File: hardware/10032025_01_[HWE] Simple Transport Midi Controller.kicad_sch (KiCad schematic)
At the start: 0 parts

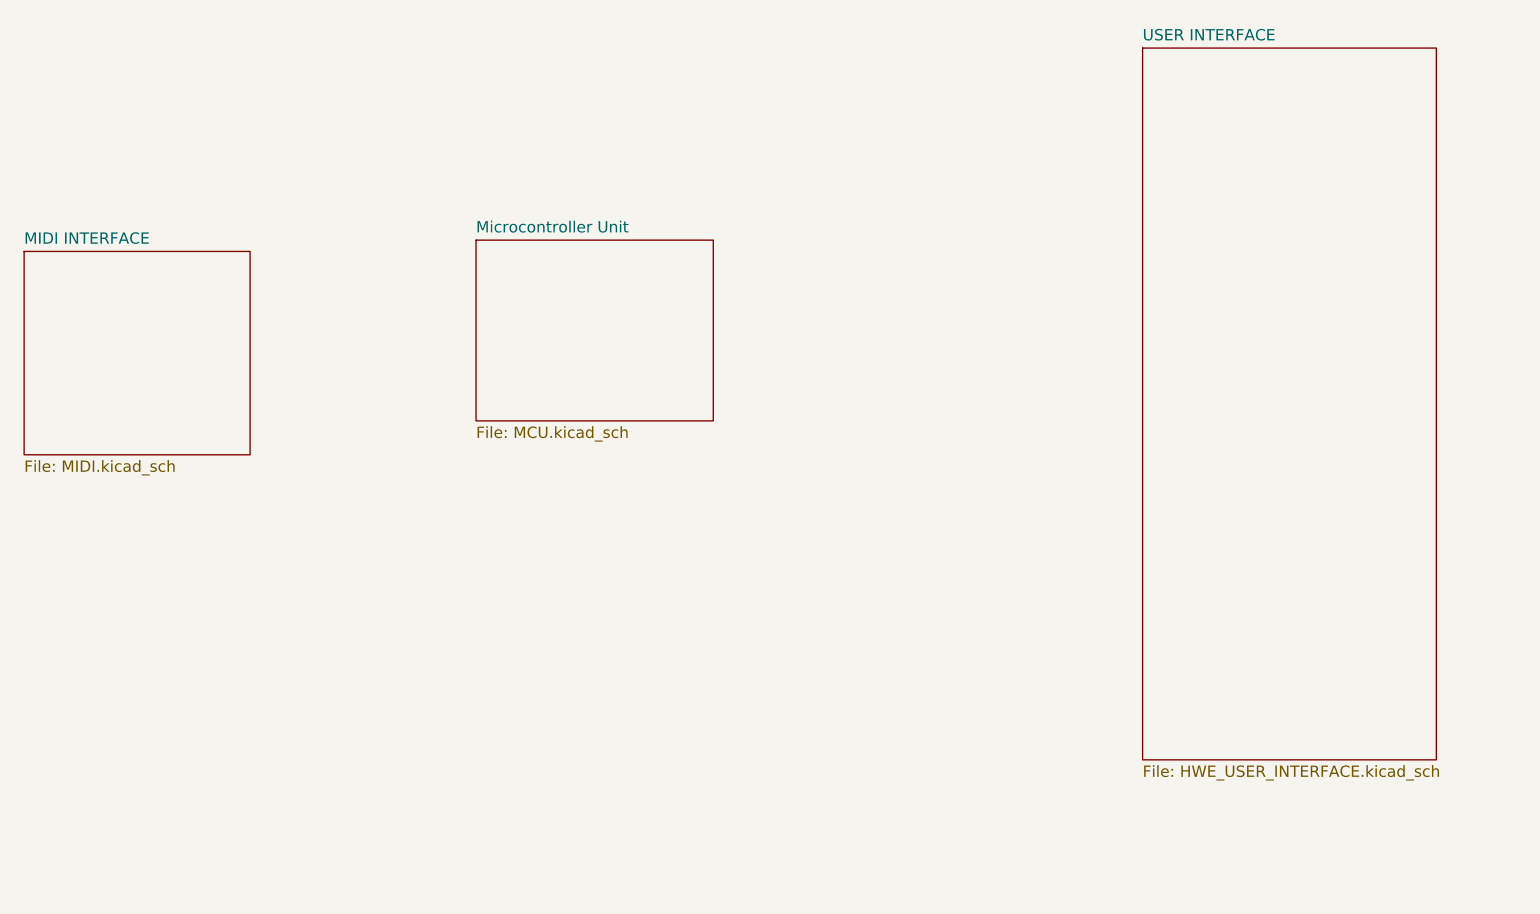
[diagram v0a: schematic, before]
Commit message: feat: Created Button I2C Interfaces
For now, all we are using is generic 1x5 Connectors following the DFR Robot's RGB Button pinout https://wiki.dfrobot.com/SKU_DFR0991_Gravity_I2C_RGB_LED_Button_Module#target_9
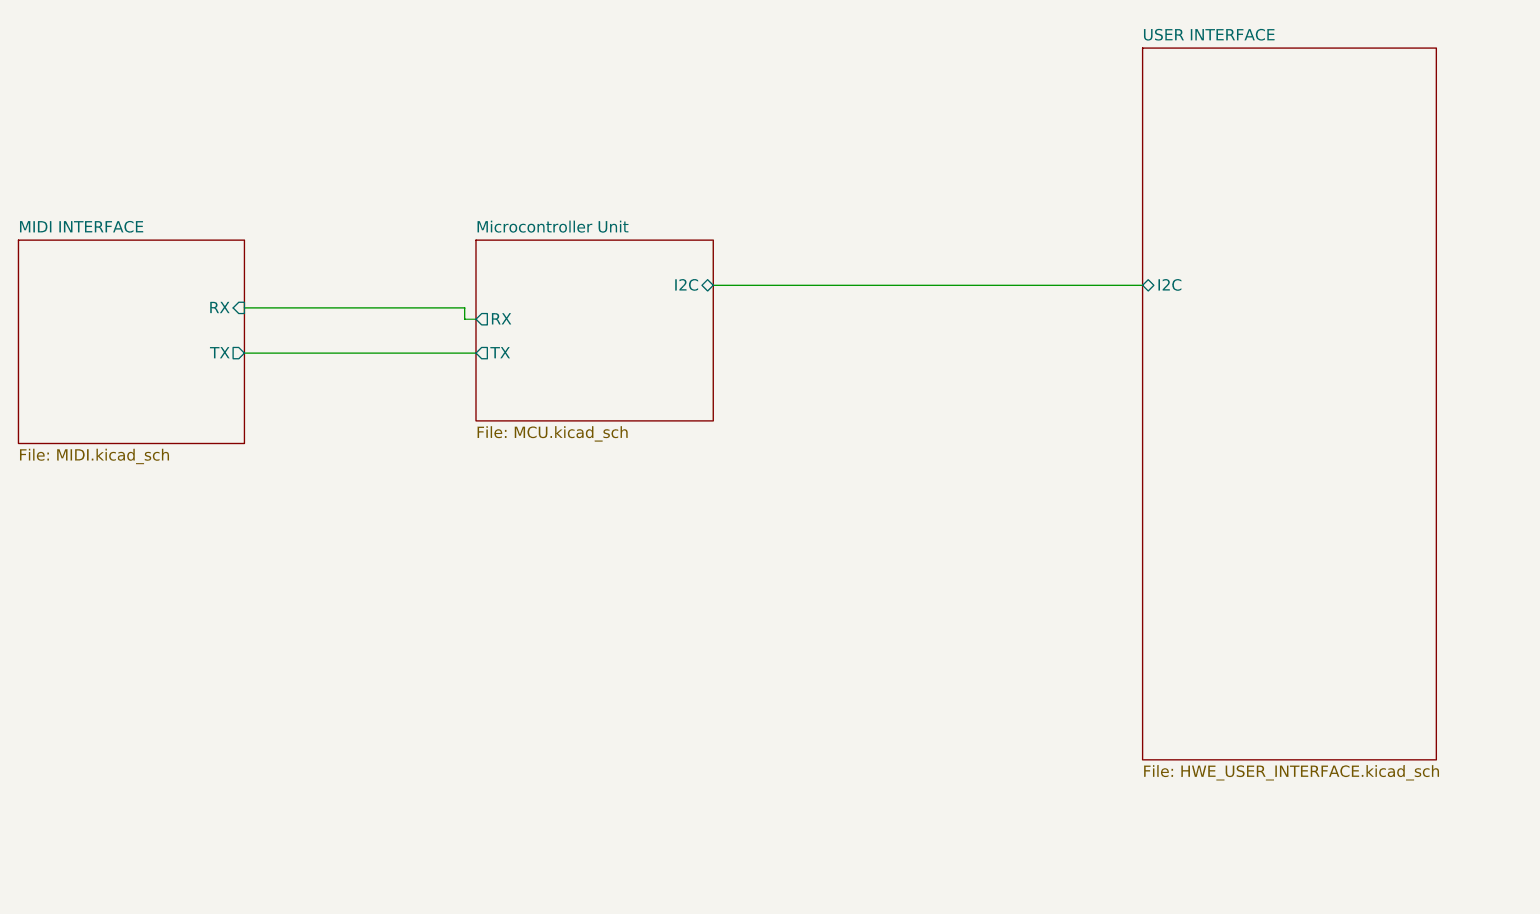
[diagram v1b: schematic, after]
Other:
- sheet MIDI INTERFACE ports: added RX, TX; removed none
- sheet Microcontroller Unit ports: added I2C, RX, TX; removed none
- sheet USER INTERFACE ports: added I2C; removed none
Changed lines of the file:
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@@
 	(generator_version "9.0")
 	(paper "A4")
+	(wire
+		(pts
+			(xy 87.63 77.47) (xy 88.9 77.47)
+		)
+		(stroke
+			(width 0)
+			(type default)
+		)
+	)
+	(wire
+		(pts
+			(xy 87.63 77.47) (xy 87.63 76.2)
+		)
+		(stroke
+			(width 0)
+			(type default)
+		)
+	)
+	(wire
+		(pts
+			(xy 115.57 73.66) (xy 163.83 73.66)
+		)
+		(stroke
+			(width 0)
+			(type default)
+		)
+	)
+	(wire
+		(pts
+			(xy 87.63 76.2) (xy 62.865 76.2)
+		)
+		(stroke
+			(width 0)
+			(type default)
+		)
+	)
+	(wire
+		(pts
+			(xy 62.865 81.28) (xy 88.9 81.28)
+		)
+		(stroke
+			(width 0)
+			(type default)
+		)
+	)
 	(sheet
-		(at 38.1 69.85)
+		(at 37.465 68.58)
 		(size 25.4 22.86)
 		(exclude_from_sim no)
@@
 		)
 		(property "Sheetname" "MIDI INTERFACE"
-			(at 38.1 69.1384 0)
+			(at 37.465 67.8684 0)
 			(effects
 				(font
@@
 		)
 		(property "Sheetfile" "MIDI.kicad_sch"
-			(at 38.1 93.2946 0)
+			(at 37.465 92.0246 0)
 			(effects
 				(font
@@
 				)
 				(justify left top)
+			)
+		)
+		(pin "RX" input
+			(at 62.865 76.2 0)
+			(effects
+				(font
+					(size 1.27 1.27)
+				)
+				(justify right)
+			)
+		)
+		(pin "TX" output
+			(at 62.865 81.28 0)
+			(effects
+				(font
+					(size 1.27 1.27)
+				)
+				(justify right)
 			)
 		)
@@
 			)
 		)
+		(pin "I2C" bidirectional
+			(at 115.57 73.66 0)
+			(effects
+				(font
+					(size 1.27 1.27)
+				)
+				(justify right)
+			)
+		)
+		(pin "RX" output
+			(at 88.9 77.47 180)
+			(effects
+				(font
+					(size 1.27 1.27)
+				)
+				(justify left)
+			)
+		)
+		(pin "TX" output
+			(at 88.9 81.28 180)
+			(effects
+				(font
+					(size 1.27 1.27)
+				)
+				(justify left)
+			)
+		)
 		(instances
 			(project "10032025_01_[HWE] Simple Transport Midi Controller"
@@
 			)
 		)
+		(pin "I2C" bidirectional
+			(at 163.83 73.66 180)
+			(effects
+				(font
+					(size 1.27 1.27)
+				)
+				(justify left)
+			)
+		)

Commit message: feat: Added Volume and Inf Scroll Encoders
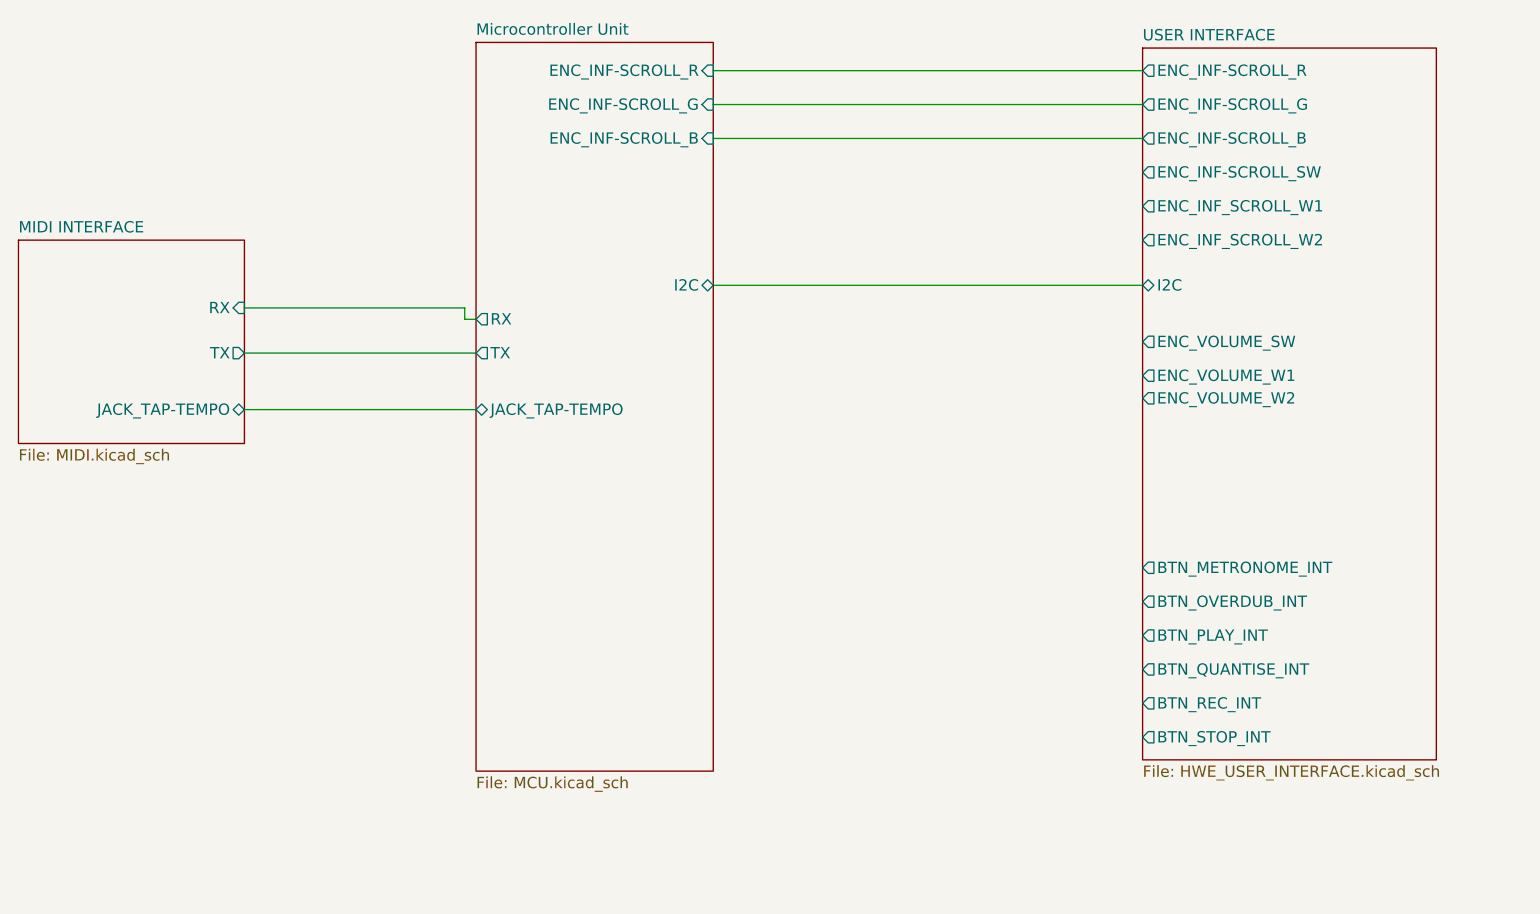
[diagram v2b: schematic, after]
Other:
- sheet MIDI INTERFACE ports: added JACK_TAP-TEMPO; removed none
- sheet Microcontroller Unit ports: added ENC_INF-SCROLL_B, ENC_INF-SCROLL_G, ENC_INF-SCROLL_R, JACK_TAP-TEMPO; removed none
- sheet USER INTERFACE ports: added BTN_METRONOME_INT, BTN_OVERDUB_INT, BTN_PLAY_INT, BTN_QUANTISE_INT, BTN_REC_INT, BTN_STOP_INT, ENC_INF-SCROLL_B, ENC_INF-SCROLL_G, ENC_INF-SCROLL_R, ENC_INF-SCROLL_SW, ENC_INF_SCROLL_W1, ENC_INF_SCROLL_W2, ENC_VOLUME_SW, ENC_VOLUME_W1, ENC_VOLUME_W2; removed none
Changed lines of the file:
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@@
+	(wire
+		(pts
+			(xy 62.865 87.63) (xy 88.9 87.63)
+		)
+		(stroke
+			(width 0)
+			(type default)
+		)
+	)
 	(wire
 		(pts
@@
 		(pts
 			(xy 87.63 76.2) (xy 62.865 76.2)
+		)
+		(stroke
+			(width 0)
+			(type default)
+		)
+	)
+	(wire
+		(pts
+			(xy 115.57 53.34) (xy 163.83 53.34)
+		)
+		(stroke
+			(width 0)
+			(type default)
+		)
+	)
+	(wire
+		(pts
+			(xy 115.57 49.53) (xy 163.83 49.53)
+		)
+		(stroke
+			(width 0)
+			(type default)
+		)
+	)
+	(wire
+		(pts
+			(xy 115.57 57.15) (xy 163.83 57.15)
 		)
 		(stroke
@@
 			)
 		)
+		(pin "JACK_TAP-TEMPO" bidirectional
+			(at 62.865 87.63 0)
+			(effects
+				(font
+					(size 1.27 1.27)
+				)
+				(justify right)
+			)
+		)
 		(instances
 			(project "10032025_01_[HWE] Simple Transport Midi Controller"
@@
 	)
 	(sheet
-		(at 88.9 68.58)
-		(size 26.67 20.32)
+		(at 88.9 46.355)
+		(size 26.67 81.915)
 		(exclude_from_sim no)
 		(in_bom yes)
@@
 		)
 		(property "Sheetname" "Microcontroller Unit"
-			(at 88.9 67.8684 0)
+			(at 88.9 45.6434 0)
 			(effects
 				(font
@@
 		)
 		(property "Sheetfile" "MCU.kicad_sch"
-			(at 88.9 89.4846 0)
+			(at 88.9 128.8546 0)
 			(effects
 				(font
@@
 		(pin "TX" output
 			(at 88.9 81.28 180)
+			(effects
+				(font
+					(size 1.27 1.27)
+				)
+				(justify left)
+			)
+		)
+		(pin "ENC_INF-SCROLL_B" input
+			(at 115.57 57.15 0)
+			(effects
+				(font
+					(size 1.27 1.27)
+				)
+				(justify right)
+			)
+		)
+		(pin "ENC_INF-SCROLL_G" input
+			(at 115.57 53.34 0)
+			(effects
+				(font
+					(size 1.27 1.27)
+				)
+				(justify right)
+			)
+		)
+		(pin "ENC_INF-SCROLL_R" input
+			(at 115.57 49.53 0)
+			(effects
+				(font
+					(size 1.27 1.27)
+				)
+				(justify right)
+			)
+		)
+		(pin "JACK_TAP-TEMPO" bidirectional
+			(at 88.9 87.63 180)
 			(effects
 				(font
@@
 			(effects
 				(font
+					(size 1.27 1.27)
+				)
+				(justify left)
+			)
+		)
+		(pin "BTN_METRONOME_INT" output
+			(at 163.83 105.41 180)
+			(effects
+				(font
+					(size 1.27 1.27)
+				)
+				(justify left)
+			)
+		)
+		(pin "BTN_OVERDUB_INT" output
+			(at 163.83 109.22 180)
+			(effects
+				(font
+					(size 1.27 1.27)
+				)
+				(justify left)
+			)
+		)
+		(pin "BTN_PLAY_INT" output
+			(at 163.83 113.03 180)
+			(effects
+				(font
+					(size 1.27 1.27)
+				)
+				(justify left)
+			)
+		)
+		(pin "BTN_QUANTISE_INT" output
+			(at 163.83 116.84 180)
+			(effects
+				(font
+					(size 1.27 1.27)
+				)
+				(justify left)
+			)
+		)
+		(pin "BTN_REC_INT" output
+			(at 163.83 120.65 180)
+			(effects
+				(font
+					(size 1.27 1.27)
+				)
+				(justify left)
+			)
+		)
+		(pin "BTN_STOP_INT" output
+			(at 163.83 124.46 180)
+			(effects
+				(font
+					(size 1.27 1.27)
+				)
+				(justify left)
+			)
+		)
+		(pin "ENC_INF-SCROLL_B" output
+			(at 163.83 57.15 180)
+			(effects
+				(font
+					(size 1.27 1.27)
+				)
+				(justify left)
+			)
+		)
+		(pin "ENC_INF-SCROLL_G" output
+			(at 163.83 53.34 180)
+			(effects
+				(font
+					(size 1.27 1.27)
+				)
+				(justify left)
+			)
+		)
+		(pin "ENC_INF-SCROLL_R" output
+			(at 163.83 49.53 180)
+			(effects
+				(font
+					(size 1.27 1.27)
+				)
+				(justify left)
+			)
+		)
+		(pin "ENC_INF-SCROLL_SW" output
+			(at 163.83 60.96 180)
+			(effects
+				(font
+					(size 1.27 1.27)
+				)
+				(justify left)
+			)
+		)
+		(pin "ENC_INF_SCROLL_W1" output
+			(at 163.83 64.77 180)
+			(effects
+				(font
+					(size 1.27 1.27)
+				)
+				(justify left)
+			)
+		)
+		(pin "ENC_INF_SCROLL_W2" output
+			(at 163.83 68.58 180)
+			(effects
+				(font
+					(size 1.27 1.27)
+				)
+				(justify left)
+			)
+		)
+		(pin "ENC_VOLUME_SW" output
+			(at 163.83 80.01 180)
+			(effects
+				(font
+					(size 1.27 1.27)
+				)
+				(justify left)
+			)
+		)
+		(pin "ENC_VOLUME_W1" output
+			(at 163.83 83.82 180)
+			(effects
+				(font
+					(size 1.27 1.27)
+				)
+				(justify left)
+			)
+		)
+		(pin "ENC_VOLUME_W2" output
+			(at 163.83 86.36 180)
+			(effects
+				(font

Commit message: feat: Connected main HW UI components to MCU
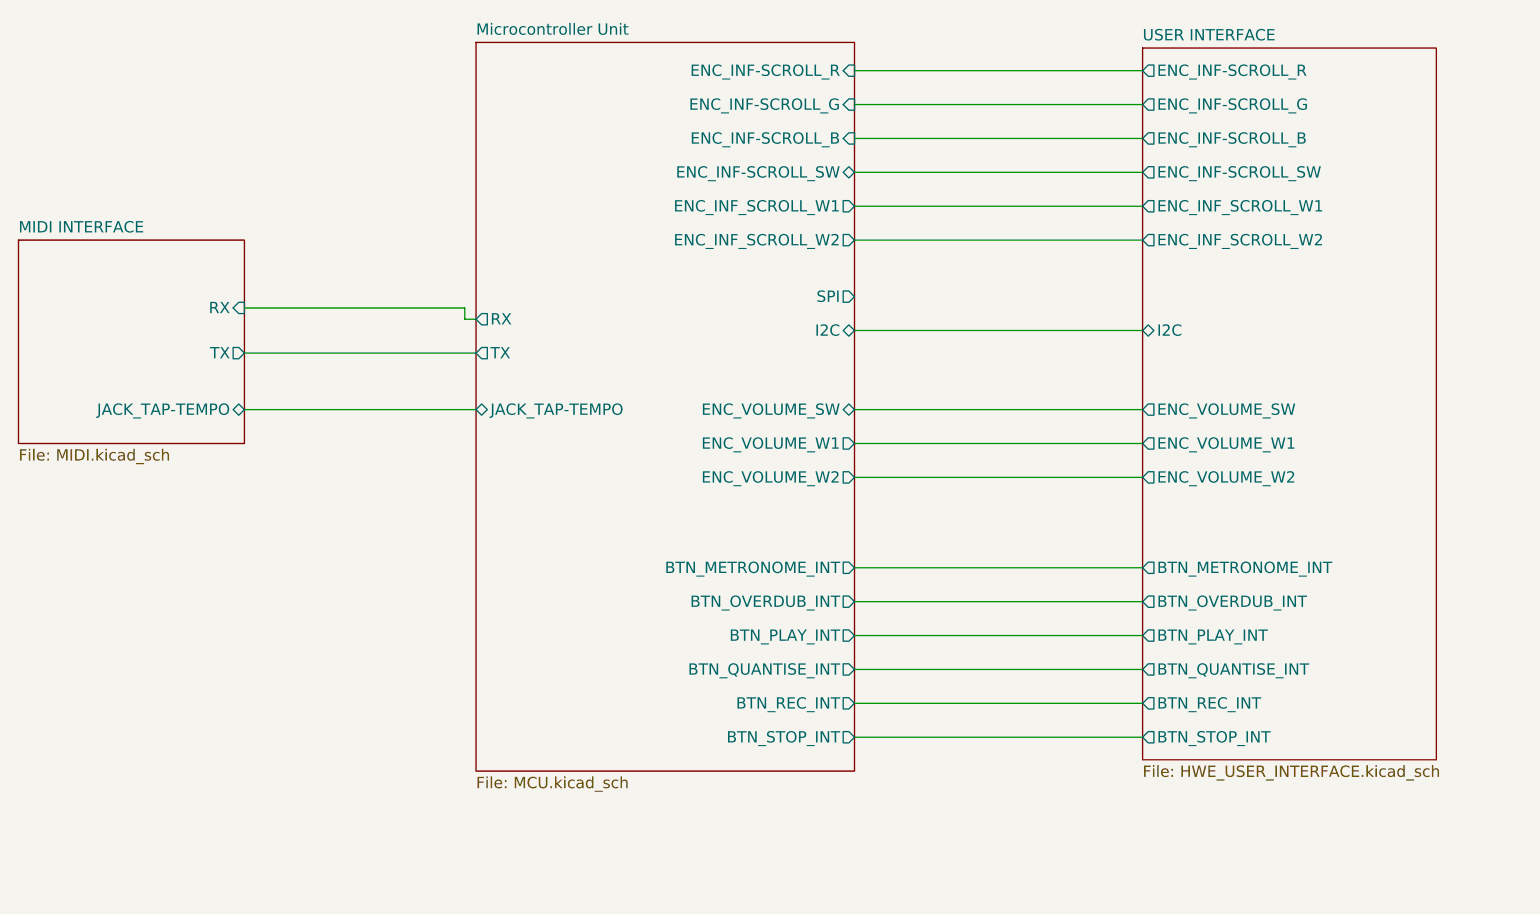
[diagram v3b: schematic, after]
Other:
- sheet Microcontroller Unit ports: added BTN_METRONOME_INT, BTN_OVERDUB_INT, BTN_PLAY_INT, BTN_QUANTISE_INT, BTN_REC_INT, BTN_STOP_INT, ENC_INF-SCROLL_SW, ENC_INF_SCROLL_W1, ENC_INF_SCROLL_W2, ENC_VOLUME_SW, ENC_VOLUME_W1, ENC_VOLUME_W2, SPI; removed none

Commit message: feat [HWE}; Added SPI Oled and refactor DuPPa LED
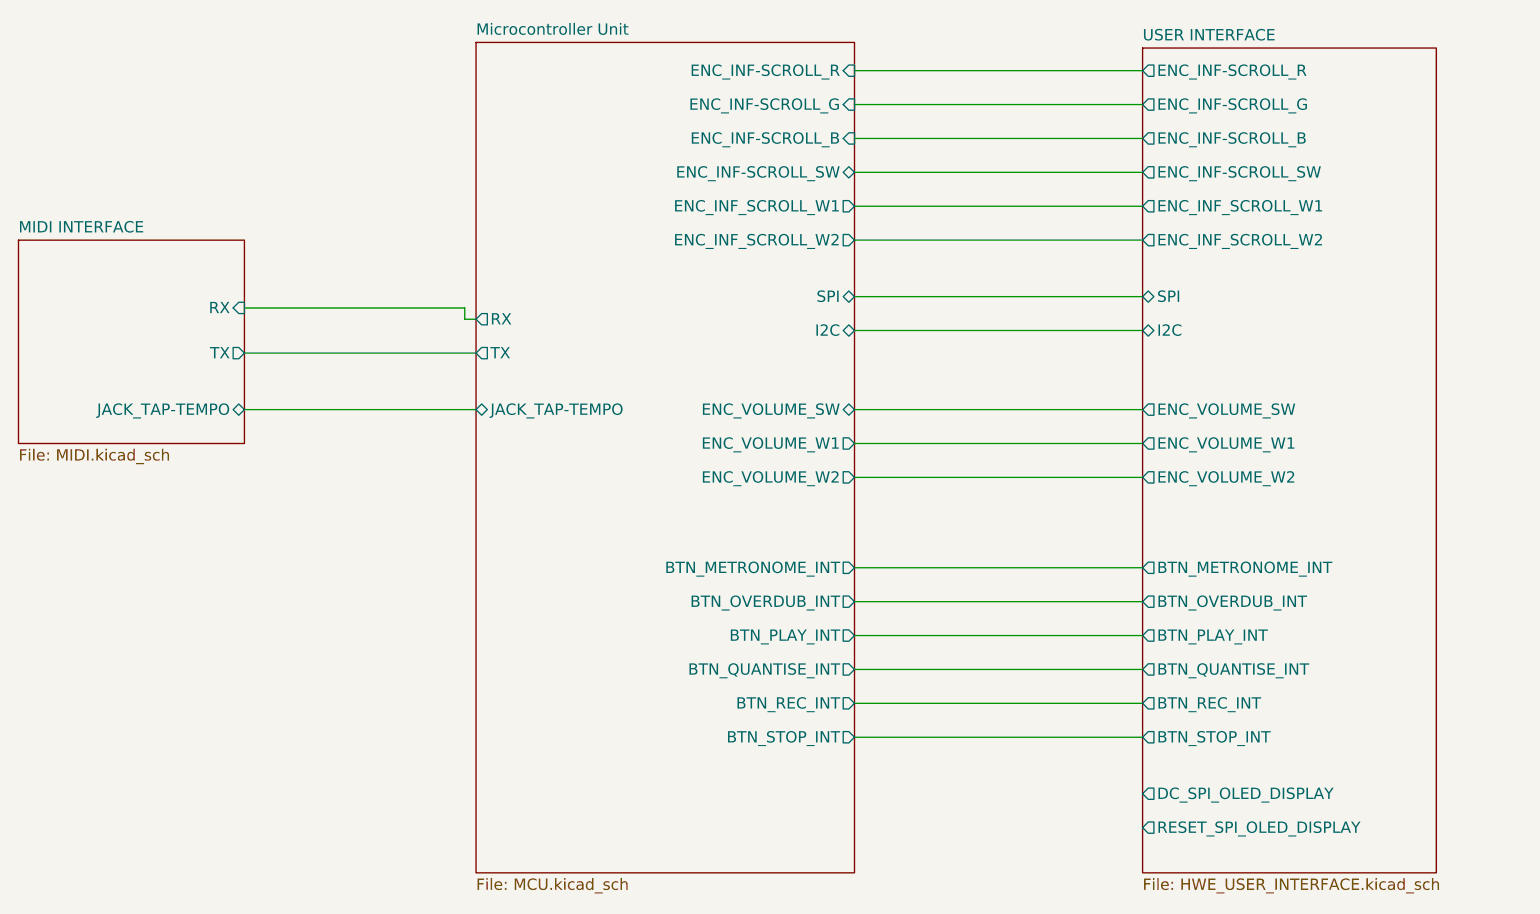
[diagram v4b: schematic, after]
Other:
- sheet USER INTERFACE ports: added DC_SPI_OLED_DISPLAY, RESET_SPI_OLED_DISPLAY, SPI; removed none
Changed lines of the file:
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@@
+	(wire
+		(pts
+			(xy 131.445 74.93) (xy 163.83 74.93)
+		)
+		(stroke
+			(width 0)
+			(type default)
+		)
+	)
 	(wire
 		(pts
@@
 	(sheet
 		(at 88.9 46.355)
-		(size 42.545 81.915)
+		(size 42.545 93.345)
 		(exclude_from_sim no)
 		(in_bom yes)
@@
 		)
 		(property "Sheetfile" "MCU.kicad_sch"
-			(at 88.9 128.8546 0)
+			(at 88.9 140.2846 0)
 			(effects
 				(font
@@
 			)
 		)
-		(pin "SPI" output
+		(pin "SPI" bidirectional
 			(at 131.445 74.93 0)
 			(effects
@@
 	(sheet
 		(at 163.83 46.99)
-		(size 33.02 80.01)
+		(size 33.02 92.71)
 		(exclude_from_sim no)
 		(in_bom yes)
@@
 		)
 		(property "Sheetfile" "HWE_USER_INTERFACE.kicad_sch"
-			(at 163.83 127.5846 0)
+			(at 163.83 140.2846 0)
 			(effects
 				(font
@@
 			(effects
 				(font
+					(size 1.27 1.27)
+				)
+				(justify left)
+			)
+		)
+		(pin "SPI" bidirectional
+			(at 163.83 74.93 180)
+			(effects
+				(font
+					(size 1.27 1.27)
+				)
+				(justify left)
+			)
+		)
+		(pin "DC_SPI_OLED_DISPLAY" output
+			(at 163.83 130.81 180)
+			(effects
+				(font
+					(size 1.27 1.27)
+				)
+				(justify left)
+			)
+		)
+		(pin "RESET_SPI_OLED_DISPLAY" output
+			(at 163.83 134.62 180)
+			(effects
+				(font
